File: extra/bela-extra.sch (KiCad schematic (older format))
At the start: 17 parts

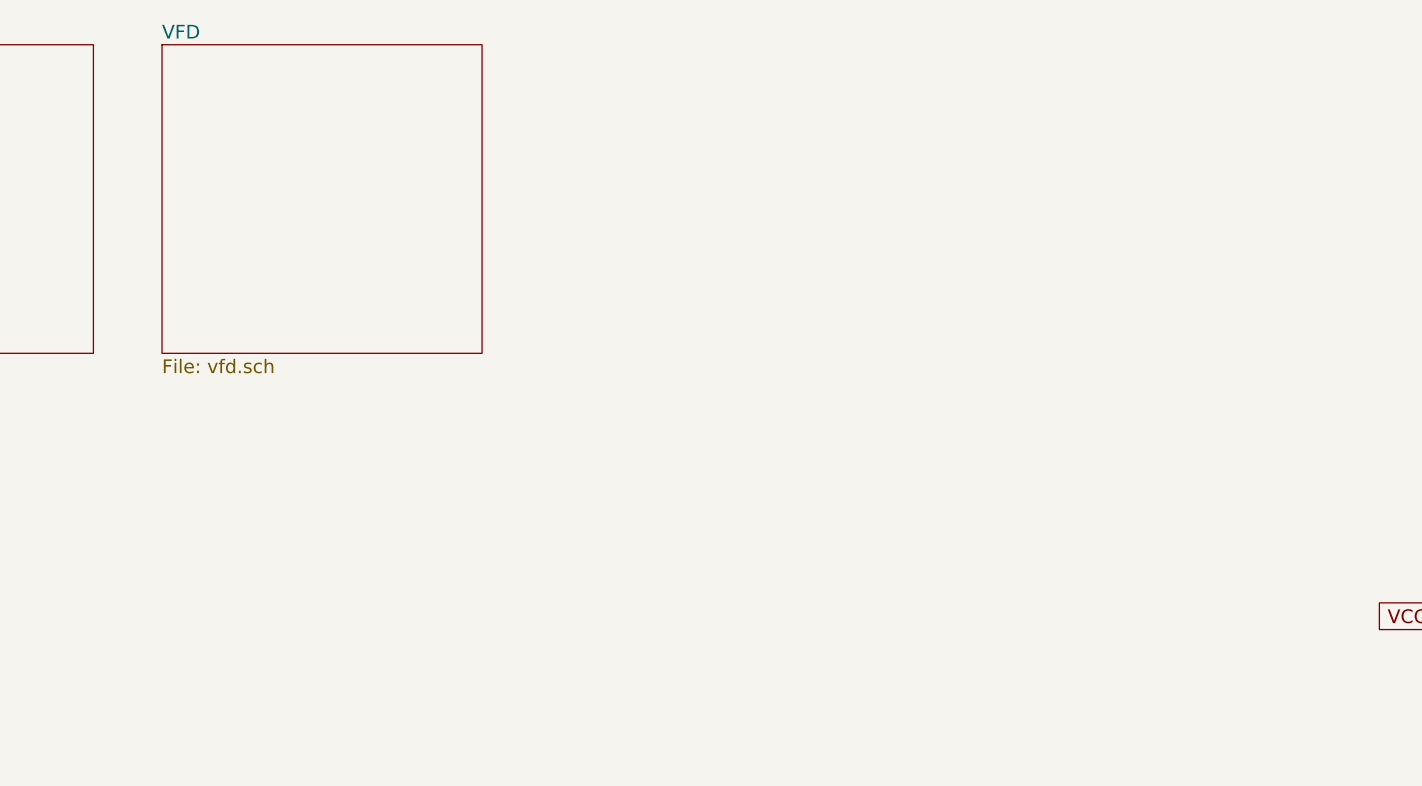
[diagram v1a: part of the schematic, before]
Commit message: much more work on vfd [2 parallel interfaces]
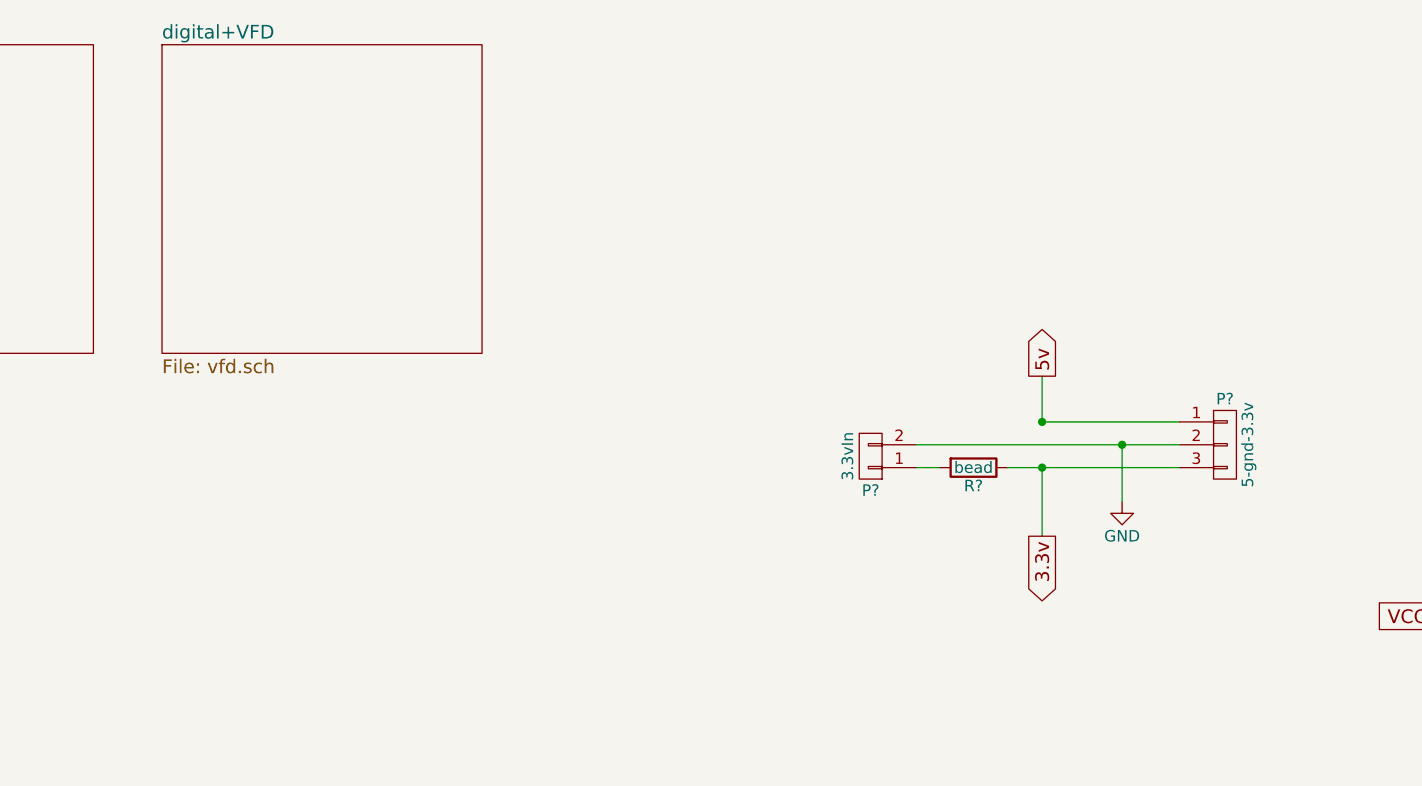
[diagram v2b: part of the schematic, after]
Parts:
- added P?: 5-gnd-3.3v, symbol CONN_01X03
- added P?: 3.3vIn, symbol CONN_01X02
- added R?: bead, Resistors_ThroughHole:Resistor_Vertical_RM5mm, symbol R
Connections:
- net 5v: now also P?.1 (P1)
- net GND: now also P?.2 (P2), P?.2 (P2)
- new net: P?.1 (P1), R?.2
- new net 3.3v: P?.3 (P3), R?.1
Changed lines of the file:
@@
 S 2300 650  1400 1350
 U 5857881D
-F0 "VFD" 60
+F0 "digital+VFD" 60
 F1 "vfd.sch" 60
 $EndSheet
+$Comp
+L CONN_01X03 P?
+U 1 1 586AB2AB
+P 6950 2400
+F 0 "P?" H 6950 2600 50  0000 C CNN
+F 1 "5-gnd-3.3v" V 7050 2400 50  0000 C CNN
+F 2 "" H 6950 2400 50  0000 C CNN
+F 3 "" H 6950 2400 50  0000 C CNN
+	1    6950 2400
+	1    0    0    -1
+$EndComp
+Wire Wire Line
+	6750 2400 5600 2400
+Text GLabel 6150 2100 1    60   Output ~ 0
+5v
+Wire Wire Line
+	6150 2100 6150 2300
+Connection ~ 6150 2300
+Text GLabel 6150 2800 3    60   Output ~ 0
+3.3v
+Wire Wire Line
+	6150 2500 6150 2800
+Connection ~ 6150 2500
+$Comp
+L R R?
+U 1 1 586AB740
+P 5850 2500
+F 0 "R?" V 5930 2500 50  0000 C CNN
+F 1 "bead" V 5850 2500 50  0000 C CNN
+F 2 "Resistors_ThroughHole:Resistor_Vertical_RM5mm" V 5780 2500 50  0001 C CNN
+F 3 "" H 5850 2500 50  0000 C CNN
+	1    5850 2500
+	0    1    1    0
+$EndComp
+Wire Wire Line
+	5600 2500 5700 2500
+Wire Wire Line
+	6000 2500 6750 2500
+$Comp
+L GND #PWR?
+U 1 1 586AB90C
+P 6500 2650
+F 0 "#PWR?" H 6500 2400 50  0001 C CNN
+F 1 "GND" H 6500 2500 50  0000 C CNN
+F 2 "" H 6500 2650 50  0000 C CNN
+F 3 "" H 6500 2650 50  0000 C CNN
+	1    6500 2650
+	1    0    0    -1
+$EndComp
+Wire Wire Line
+	6500 2400 6500 2650
+Connection ~ 6500 2400
+$Comp
+L CONN_01X02 P?
+U 1 1 586ABAEC
+P 5400 2450
+F 0 "P?" H 5400 2600 50  0000 C CNN
+F 1 "3.3vIn" V 5500 2450 50  0000 C CNN
+F 2 "" H 5400 2450 50  0000 C CNN
+F 3 "" H 5400 2450 50  0000 C CNN
+	1    5400 2450
+	-1   0    0    1
+$EndComp
+Wire Wire Line
+	6150 2300 6750 2300
 $EndSCHEMATC

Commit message: a bunch more hooking up
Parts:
- added P?: bbp9, symbol CONN_02X23
- added P?: bbbp8, symbol CONN_02X23
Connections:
- net GND: now also P?.1 (P1), P?.2 (P2)
- new net bb-vfd-RD+RW: P?.37 (P37)
- new net bb-vfd-WR+RS: P?.38 (P38)
- new net bb-vfdCS1: P?.36 (P36)
- new net bb-vfdCS2: P?.35 (P35)
- new net bb-vfdD0: P?.46 (P46)
- new net bb-vfdD1: P?.45 (P45)
- new net bb-vfdD2: P?.44 (P44)
- new net bb-vfdD3: P?.43 (P43)
- new net bb-vfdD4: P?.42 (P42)
- new net bb-vfdD5: P?.41 (P41)
- new net bb-vfdD6: P?.40 (P40)
- new net bb-vfdD7: P?.39 (P39)
- new net bb-vfdD7enable: P?.32 (P32)
- new net bb-vfdE: P?.34 (P34)
- new net bb-vfdpBusy: P?.31 (P31)
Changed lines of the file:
@@
 $EndComp
 Wire Wire Line
-	6750 2400 5600 2400
+	5600 2400 6750 2400
 Text GLabel 6150 2100 1    60   Output ~ 0
 5v
@@
 Wire Wire Line
 	6150 2300 6750 2300
+$Comp
+L CONN_02X23 P?
+U 1 1 586B0458
+P 1750 4800
+F 0 "P?" H 1750 6000 50  0000 C CNN
+F 1 "bbp9" V 1750 4800 50  0000 C CNN
+F 2 "" H 1750 3950 50  0000 C CNN
+F 3 "" H 1750 3950 50  0000 C CNN
+	1    1750 4800
+	1    0    0    -1
+$EndComp
+$Comp
+L CONN_02X23 P?
+U 1 1 586B04DD
+P 5000 4800
+F 0 "P?" H 5000 6000 50  0000 C CNN
+F 1 "bbbp8" V 5000 4800 50  0000 C CNN
+F 2 "" H 5000 3950 50  0000 C CNN
+F 3 "" H 5000 3950 50  0000 C CNN
+	1    5000 4800
+	1    0    0    -1
+$EndComp
+$Comp
+L GND #PWR?
+U 1 1 586B08A6
+P 5800 3700
+F 0 "#PWR?" H 5800 3450 50  0001 C CNN
+F 1 "GND" H 5800 3550 50  0000 C CNN
+F 2 "" H 5800 3700 50  0000 C CNN
+F 3 "" H 5800 3700 50  0000 C CNN
+	1    5800 3700
+	1    0    0    -1
+$EndComp
+Wire Wire Line
+	5250 3700 5800 3700
+Wire Wire Line
+	4750 3700 4750 3550
+Wire Wire Line
+	4750 3550 5300 3550
+Wire Wire Line
+	5300 3550 5300 3700
+Connection ~ 5300 3700
+Text GLabel 5300 5200 2    60   Output ~ 0
+bb-vfdD7enable
+Text GLabel 5350 5900 2    60   Output ~ 0
+bb-vfdD0
+Text GLabel 4650 5900 0    60   Output ~ 0
+bb-vfdD1
+Text GLabel 5350 5800 2    60   Output ~ 0
+bb-vfdD2
+Text GLabel 4650 5800 0    60   Output ~ 0
+bb-vfdD3
+Text GLabel 5350 5700 2    60   Output ~ 0
+bb-vfdD4
+Text GLabel 4650 5700 0    60   Output ~ 0
+bb-vfdD5
+Text GLabel 5350 5600 2    60   Output ~ 0
+bb-vfdD6
+Text GLabel 4650 5600 0    60   Output ~ 0
+bb-vfdD7
+Wire Wire Line
+	5250 5900 5350 5900
+Wire Wire Line
+	5350 5800 5250 5800
+Wire Wire Line
+	5250 5700 5350 5700
+Wire Wire Line
+	5250 5600 5350 5600
+Wire Wire Line
+	4750 5600 4650 5600
+Wire Wire Line
+	4650 5700 4750 5700
+Wire Wire Line
+	4750 5800 4650 5800
+Wire Wire Line
+	4650 5900 4750 5900
+Text GLabel 5300 5500 2    60   Output ~ 0
+bb-vfd-WR+RS
+Text GLabel 4700 5500 0    60   Output ~ 0
+bb-vfd-RD+RW
+Text GLabel 5300 5400 2    60   Output ~ 0
+bb-vfdCS1
+Text GLabel 4700 5400 0    60   Output ~ 0
+bb-vfdCS2
+Wire Wire Line
+	4750 5500 4700 5500
+Wire Wire Line
+	5250 5500 5300 5500
+Wire Wire Line
+	4750 5400 4700 5400
+Wire Wire Line
+	5250 5400 5300 5400
+Text GLabel 5300 5300 2    60   Output ~ 0
+bb-vfdE
+Wire Wire Line
+	5300 5300 5250 5300
+Text GLabel 4650 5200 0    60   Input ~ 0
+bb-vfdpBusy
+Wire Wire Line
+	5250 5200 5300 5200
+Wire Wire Line
+	4650 5200 4750 5200
 $EndSCHEMATC

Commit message: a lot more layout work
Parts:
- removed P?: 5-gnd-3.3v, symbol CONN_01X03
- removed P?: 3.3vIn, symbol CONN_01X02
- removed R?: bead, Resistors_ThroughHole:Resistor_Vertical_RM5mm, symbol R
- added P3: enc+btn1, symbol CONN_01X04
- added P4: enc+btn2, symbol CONN_01X04
- added R1: bead, xnorman:Resistor_Vertical_RM5mm-xnor, symbol R
- R2, R3, R4: renamed from R?; footprint Resistors_ThroughHole:Resistor_Vertical_RM5mm -> xnorman:Resistor_Vertical_RM5mm-xnor
- gave numbers to parts that had none: 16
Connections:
- net 3.3v: now also R1.1
- net GND: now also P3.4 (P4), P4.4 (P4)
- net encin2-btn: now reaches P1.12 (P12)
- net encin2-btn: now also P4.3 (P3)
- net encin2-b: now reaches P1.14 (P14)
- net encin2-b: now also P4.2 (P2)
- net encin2-a: now reaches P1.16 (P16)
- net encin2-a: now also P4.1 (P1)
- net at P1.4 (P4): now also R1.2
- net beladigin4: now reaches P2.10 (P10)
- net beladigin5: now reaches P2.11 (P11)
- net beladigin6: now reaches P2.12 (P12)
- net beladigout1: now reaches P2.15 (P15)
- net beladigout2: now reaches P2.16 (P16)
- net beladigout3: now reaches P2.18 (P18)
- net encin1-btn: now reaches P2.20 (P20)
- net encin1-btn: now also P3.3 (P3)
- net encin1-b: now reaches P2.22 (P22)
- net encin1-b: now also P3.2 (P2)
- net encin1-a: now reaches P2.24 (P24)
- net encin1-a: now also P3.1 (P1)
- net beladigout5: now reaches P2.27 (P27)
- net beladigout4: now reaches P2.28 (P28)
- net beladigout7: now reaches P2.29 (P29)
- net beladigout6: now reaches P2.30 (P30)
- net beladigin1: now reaches P2.7 (P7)
- net beladigin2: now reaches P2.8 (P8)
- net beladigin3: now reaches P2.9 (P9)
- no-connect marks 0 -> 55
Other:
- note added: "enc1 not mapped to bela digital"
- note added: "enc2 is mapped to bela digital"

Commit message: starting pcb layout a little
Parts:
- D1: footprint (none) -> Diodes_ThroughHole:Diode_DO-41_SOD81_Horizontal_RM10
- P1, P2: footprint (none) -> Pin_Headers:Pin_Header_Straight_2x23_Pitch2.54mm
- P3, P4: footprint (none) -> Pin_Headers:Pin_Header_Straight_1x03_Pitch2.54mm
- P6: footprint (none) -> Pin_Headers:Pin_Header_Angled_1x02_Pitch2.54mm
- U2: footprint (none) -> TO_SOT_Packages_THT:TO-220_Neutral123_Vertical_LargePads
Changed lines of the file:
@@
 F 0 "U2" H 9500 3004 50  0000 C CNN
 F 1 "LM78S05" H 9350 3400 50  0000 C CNN
-F 2 "" H 9350 3200 50  0001 C CNN
+F 2 "TO_SOT_Packages_THT:TO-220_Neutral123_Vertical_LargePads" H 9350 3200 50  0001 C CNN
 F 3 "" H 9350 3200 50  0000 C CNN
 	1    9350 3200
@@
 F 0 "D1" H 8400 3250 50  0000 C CNN
 F 1 "1N5400" H 8400 3050 50  0000 C CNN
-F 2 "" H 8400 3150 50  0001 C CNN
+F 2 "Diodes_ThroughHole:Diode_DO-41_SOD81_Horizontal_RM10" H 8400 3150 50  0001 C CNN
 F 3 "" H 8400 3150 50  0000 C CNN
 	1    8400 3150
@@
 F 0 "P6" H 10800 3700 50  0000 C CNN
 F 1 "bela_power" V 10900 3550 50  0000 C CNN
-F 2 "" H 10800 3550 50  0001 C CNN
+F 2 "Pin_Headers:Pin_Header_Angled_1x02_Pitch2.54mm" H 10800 3550 50  0001 C CNN
 F 3 "" H 10800 3550 50  0000 C CNN
 	1    10800 3550
@@
 F 0 "P1" H 1750 6000 50  0000 C CNN
 F 1 "bbp9" V 1750 4800 50  0000 C CNN
-F 2 "" H 1750 3950 50  0001 C CNN
+F 2 "Pin_Headers:Pin_Header_Straight_2x23_Pitch2.54mm" H 1750 3950 50  0001 C CNN
 F 3 "" H 1750 3950 50  0000 C CNN
 	1    1750 4800
@@
 F 0 "P2" H 5000 6000 50  0000 C CNN
 F 1 "bbbp8" V 5000 4800 50  0000 C CNN
-F 2 "" H 5000 3950 50  0001 C CNN
+F 2 "Pin_Headers:Pin_Header_Straight_2x23_Pitch2.54mm" H 5000 3950 50  0001 C CNN
 F 3 "" H 5000 3950 50  0000 C CNN
 	1    5000 4800
@@
 F 0 "P3" H 6450 2150 50  0000 C CNN
 F 1 "enc+btn1" V 6550 1900 50  0000 C CNN
-F 2 "" H 6450 1900 50  0001 C CNN
+F 2 "Pin_Headers:Pin_Header_Straight_1x03_Pitch2.54mm" H 6450 1900 50  0001 C CNN
 F 3 "" H 6450 1900 50  0000 C CNN
 	1    6450 1900
@@
 F 0 "P4" H 6450 2650 50  0000 C CNN
 F 1 "enc+btn2" V 6550 2400 50  0000 C CNN
-F 2 "" H 6450 2400 50  0001 C CNN
+F 2 "Pin_Headers:Pin_Header_Straight_1x03_Pitch2.54mm" H 6450 2400 50  0001 C CNN
 F 3 "" H 6450 2400 50  0000 C CNN
 	1    6450 2400

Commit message: moving along, still no idea why 5v is hooked to 3.3v
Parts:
- removed P1: bbp9, Pin_Headers:Pin_Header_Straight_2x23_Pitch2.54mm, symbol CONN_02X23
- removed U2: LM78S05, TO_SOT_Packages_THT:TO-220_Neutral123_Vertical_LargePads, symbol LM7805
- added P1: bbbp9, Pin_Headers:Pin_Header_Straight_2x08_Pitch2.54mm, symbol CONN_02X08
- added U2: 7805-xnor, TO_SOT_Packages_THT:TO-220_Neutral123_Vertical_LargePads, symbol 7805-xnor
- P6: footprint Pin_Headers:Pin_Header_Angled_1x02_Pitch2.54mm -> Pin_Headers:Pin_Header_Straight_1x02_Pitch2.54mm
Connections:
- net 5v: now also U2.3 (VO)
- net GND: now also U2.2 (GND)
- net encin2-a: now also P1.16 (P16)
- net encin2-b: now also P1.14 (P14)
- net encin2-btn: now also P1.12 (P12)
- net at C1.1, D1.1 (K): now also U2.1 (VI)
- net at R1.2: now also P1.4 (P4)
- net VCC renamed +15v
- net VSS renamed -15v
- no-connect marks 55 -> 25
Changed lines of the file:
@@
 LIBS:contrib
 LIBS:valves
+LIBS:xnorman
 LIBS:bela-extra-cache
 EELAYER 25 0
@@
 $EndComp
 Text GLabel 9650 1250 2    60   Output ~ 0
-VCC
++15v
 Text GLabel 9650 1550 2    60   Output ~ 0
-VSS
+-15v
 $Comp
 L PWR_FLAG #FLG02
-U 1 1 58571C6E
-P 9950 1800
-F 0 "#FLG02" H 9950 1895 50  0001 C CNN
-F 1 "PWR_FLAG" H 9950 1980 50  0000 C CNN
-F 2 "" H 9950 1800 50  0000 C CNN
-F 3 "" H 9950 1800 50  0000 C CNN
-	1    9950 1800
-	0    1    1    0
-$EndComp
-$Comp
-L PWR_FLAG #FLG03
 U 1 1 58571C96
 P 9250 2050
-F 0 "#FLG03" H 9250 2145 50  0001 C CNN
+F 0 "#FLG02" H 9250 2145 50  0001 C CNN
 F 1 "PWR_FLAG" H 9250 2230 50  0000 C CNN
 F 2 "" H 9250 2050 50  0000 C CNN
@@
 	1    9250 2050
 	-1   0    0    1
-$EndComp
-$Comp
-L LM7805 U2
-U 1 1 58571DAF
-P 9350 3200
-F 0 "U2" H 9500 3004 50  0000 C CNN
-F 1 "LM78S05" H 9350 3400 50  0000 C CNN
-F 2 "TO_SOT_Packages_THT:TO-220_Neutral123_Vertical_LargePads" H 9350 3200 50  0001 C CNN
-F 3 "" H 9350 3200 50  0000 C CNN
-	1    9350 3200
-	1    0    0    -1
 $EndComp
 $Comp
@@
 $EndComp
 Text GLabel 7900 3150 0    60   Input ~ 0
-VCC
-$Comp
-L GND #PWR04
++15v
+$Comp
+L GND #PWR03
 U 1 1 58572336
 P 9200 3750
-F 0 "#PWR04" H 9200 3500 50  0001 C CNN
+F 0 "#PWR03" H 9200 3500 50  0001 C CNN
 F 1 "GND" H 9200 3600 50  0000 C CNN
 F 2 "" H 9200 3750 50  0000 C CNN
@@
 $EndComp
 Text GLabel 9550 4650 0    60   Input ~ 0
-VCC
++15v
 Text GLabel 9500 6000 0    60   Input ~ 0
-VSS
-$Comp
-L GND #PWR05
+-15v
+$Comp
+L GND #PWR04
 U 1 1 58577A62
 P 9350 5450
-F 0 "#PWR05" H 9350 5200 50  0001 C CNN
+F 0 "#PWR04" H 9350 5200 50  0001 C CNN
 F 1 "GND" H 9350 5300 50  0000 C CNN
 F 2 "" H 9350 5450 50  0000 C CNN
@@
 F 0 "P6" H 10800 3700 50  0000 C CNN
 F 1 "bela_power" V 10900 3550 50  0000 C CNN
-F 2 "Pin_Headers:Pin_Header_Angled_1x02_Pitch2.54mm" H 10800 3550 50  0001 C CNN
+F 2 "Pin_Headers:Pin_Header_Straight_1x02_Pitch2.54mm" H 10800 3550 50  0001 C CNN
 F 3 "" H 10800 3550 50  0000 C CNN
 	1    10800 3550
@@
 F1 "vfd.sch" 60
 $EndSheet
-$Comp
-L CONN_02X23 P1
-U 1 1 586B0458
-P 1750 4800
-F 0 "P1" H 1750 6000 50  0000 C CNN
-F 1 "bbp9" V 1750 4800 50  0000 C CNN
-F 2 "Pin_Headers:Pin_Header_Straight_2x23_Pitch2.54mm" H 1750 3950 50  0001 C CNN
-F 3 "" H 1750 3950 50  0000 C CNN
-	1    1750 4800
-	1    0    0    -1
-$EndComp
 $Comp
 L CONN_02X23 P2
@@
 $EndComp
 $Comp
-L GND #PWR06
+L GND #PWR05
 U 1 1 586B08A6
 P 5800 3700
-F 0 "#PWR06" H 5800 3450 50  0001 C CNN
+F 0 "#PWR05" H 5800 3450 50  0001 C CNN
 F 1 "GND" H 5800 3550 50  0000 C CNN
 F 2 "" H 5800 3700 50  0000 C CNN
@@
 encin2-a
 $Comp
-L GND #PWR07
+L GND #PWR06
 U 1 1 586C8041
 P 6150 2650
-F 0 "#PWR07" H 6150 2400 50  0001 C CNN
+F 0 "#PWR06" H 6150 2400 50  0001 C CNN
 F 1 "GND" H 6150 2500 50  0000 C CNN
 F 2 "" H 6150 2650 50  0000 C CNN
@@
 NoConn ~ 1500 4300
 NoConn ~ 1500 4400
-NoConn ~ 1500 4500
-NoConn ~ 2000 4500
-NoConn ~ 2000 4600
-NoConn ~ 2000 4700
-NoConn ~ 1500 4600
-NoConn ~ 1500 4700
-NoConn ~ 1500 4800
-NoConn ~ 1500 4900
-NoConn ~ 1500 5000
-NoConn ~ 1500 5100
-NoConn ~ 1500 5200
-NoConn ~ 1500 5300
-NoConn ~ 1500 5400
-NoConn ~ 1500 5500
-NoConn ~ 1500 5600
-NoConn ~ 1500 5700
-NoConn ~ 1500 5800
-NoConn ~ 1500 5900
-NoConn ~ 2000 5900
-NoConn ~ 2000 5800
-NoConn ~ 2000 5700
-NoConn ~ 2000 5600
-NoConn ~ 2000 5500
-NoConn ~ 2000 5400
-NoConn ~ 2000 5300
-NoConn ~ 2000 5200
-NoConn ~ 2000 5100
-NoConn ~ 2000 5000
-NoConn ~ 2000 4900
-NoConn ~ 2000 4800
 NoConn ~ 4750 3800
 NoConn ~ 4750 3900
@@
 Connection ~ 9250 1900
 Wire Wire Line
-	9600 1800 9950 1800
-Wire Wire Line
 	9350 3650 9350 3450
 Wire Wire Line
@@
 Connection ~ 8750 3150
 Wire Wire Line
-	9750 3150 10200 3150
-Wire Wire Line
-	9900 3150 9900 3200
-Connection ~ 9900 3150
-Wire Wire Line
 	7900 3150 8250 3150
 Wire Wire Line
 	9200 3750 9200 3650
 Connection ~ 9200 3650
-Wire Wire Line
-	10050 2950 10050 3150
-Connection ~ 10050 3150
 Wire Wire Line
 	9800 5300 9800 5400
@@
 Wire Wire Line
 	5250 4800 5350 4800
-Wire Wire Line
-	9600 1800 9600 1550
 Connection ~ 9600 1550
 Connection ~ 9600 1250
+$Comp
+L CONN_02X08 P1
+U 1 1 586DA958
+P 1750 4050
+F 0 "P1" H 1750 4500 50  0000 C CNN
+F 1 "bbbp9" V 1750 4050 50  0000 C CNN
+F 2 "Pin_Headers:Pin_Header_Straight_2x08_Pitch2.54mm" H 1750 2850 50  0001 C CNN
+F 3 "" H 1750 2850 50  0000 C CNN
+	1    1750 4050
+	1    0    0    -1
+$EndComp
+$Comp
+L PWR_FLAG #FLG07
+U 1 1 586DBA15
+P 9950 1050
+F 0 "#FLG07" H 9950 1145 50  0001 C CNN
+F 1 "PWR_FLAG" H 9950 1230 50  0000 C CNN
+F 2 "" H 9950 1050 50  0000 C CNN
+F 3 "" H 9950 1050 50  0000 C CNN
+	1    9950 1050
+	0    1    1    0
+$EndComp
+Wire Wire Line
+	9950 1050 9600 1050
+Wire Wire Line
+	9600 1050 9600 1250
+Wire Wire Line
+	9600 1800 9600 1550
+$Comp
+L PWR_FLAG #FLG08
+U 1 1 58571C6E
+P 9950 1800
+F 0 "#FLG08" H 9950 1895 50  0001 C CNN
+F 1 "PWR_FLAG" H 9950 1980 50  0000 C CNN
+F 2 "" H 9950 1800 50  0000 C CNN
+F 3 "" H 9950 1800 50  0000 C CNN
+	1    9950 1800
+	0    1    1    0
+$EndComp
+Wire Wire Line
+	9600 1800 9950 1800
+Wire Wire Line
+	9750 3150 10200 3150
+Wire Wire Line
+	9900 3150 9900 3200
+Connection ~ 9900 3150
+Wire Wire Line
+	10050 2950 10050 3150
+Connection ~ 10050 3150
+$Comp
+L 7805-xnor U2
+U 1 1 586E3B91
+P 9350 3200
+F 0 "U2" H 9500 3004 50  0000 C CNN
+F 1 "7805-xnor" H 9350 3400 50  0000 C CNN
+F 2 "TO_SOT_Packages_THT:TO-220_Neutral123_Vertical_LargePads" H 9350 3200 50  0001 C CNN
+F 3 "" H 9350 3200 50  0000 C CNN
+	1    9350 3200
+	1    0    0    -1
+$EndComp
 $EndSCHEMATC

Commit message: fixed up some footprint issues
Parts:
- P3, P4: footprint Pin_Headers:Pin_Header_Straight_1x03_Pitch2.54mm -> Pin_Headers:Pin_Header_Straight_1x04_Pitch2.54mm
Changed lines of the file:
@@
 F 0 "P3" H 6450 2150 50  0000 C CNN
 F 1 "enc+btn1" V 6550 1900 50  0000 C CNN
-F 2 "Pin_Headers:Pin_Header_Straight_1x03_Pitch2.54mm" H 6450 1900 50  0001 C CNN
+F 2 "Pin_Headers:Pin_Header_Straight_1x04_Pitch2.54mm" H 6450 1900 50  0001 C CNN
 F 3 "" H 6450 1900 50  0000 C CNN
 	1    6450 1900
@@
 F 0 "P4" H 6450 2650 50  0000 C CNN
 F 1 "enc+btn2" V 6550 2400 50  0000 C CNN
-F 2 "Pin_Headers:Pin_Header_Straight_1x03_Pitch2.54mm" H 6450 2400 50  0001 C CNN
+F 2 "Pin_Headers:Pin_Header_Straight_1x04_Pitch2.54mm" H 6450 2400 50  0001 C CNN
 F 3 "" H 6450 2400 50  0000 C CNN
 	1    6450 2400
